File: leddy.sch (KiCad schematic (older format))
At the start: 98 parts, among them J1 hole 1, J2 hole 1, J3 hole 1, J4 hole 1, J5 umbrella hole, J6 PJ-002AH-SMT-TR, J7 OPEN HARDWARE, Q1 ZXMP6A13GTA, SW1 PTS645SM70SMTR92, U1 LT3518EFE#PBF, U2 74HC4017PW

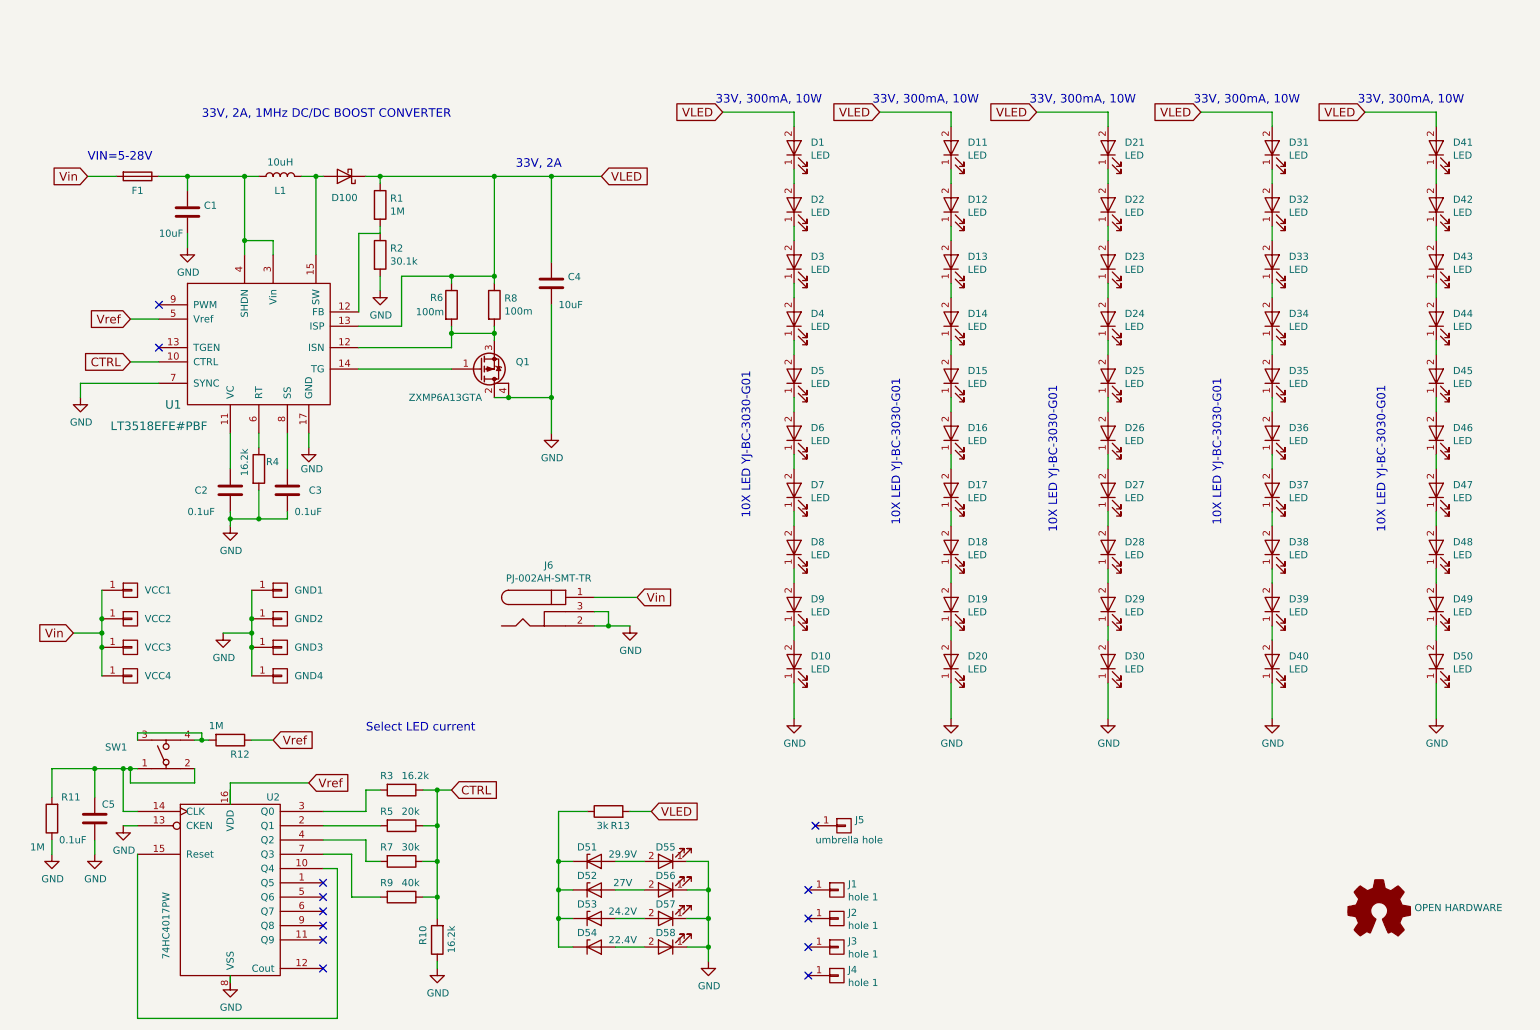
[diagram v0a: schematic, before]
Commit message: added better LED current level meter
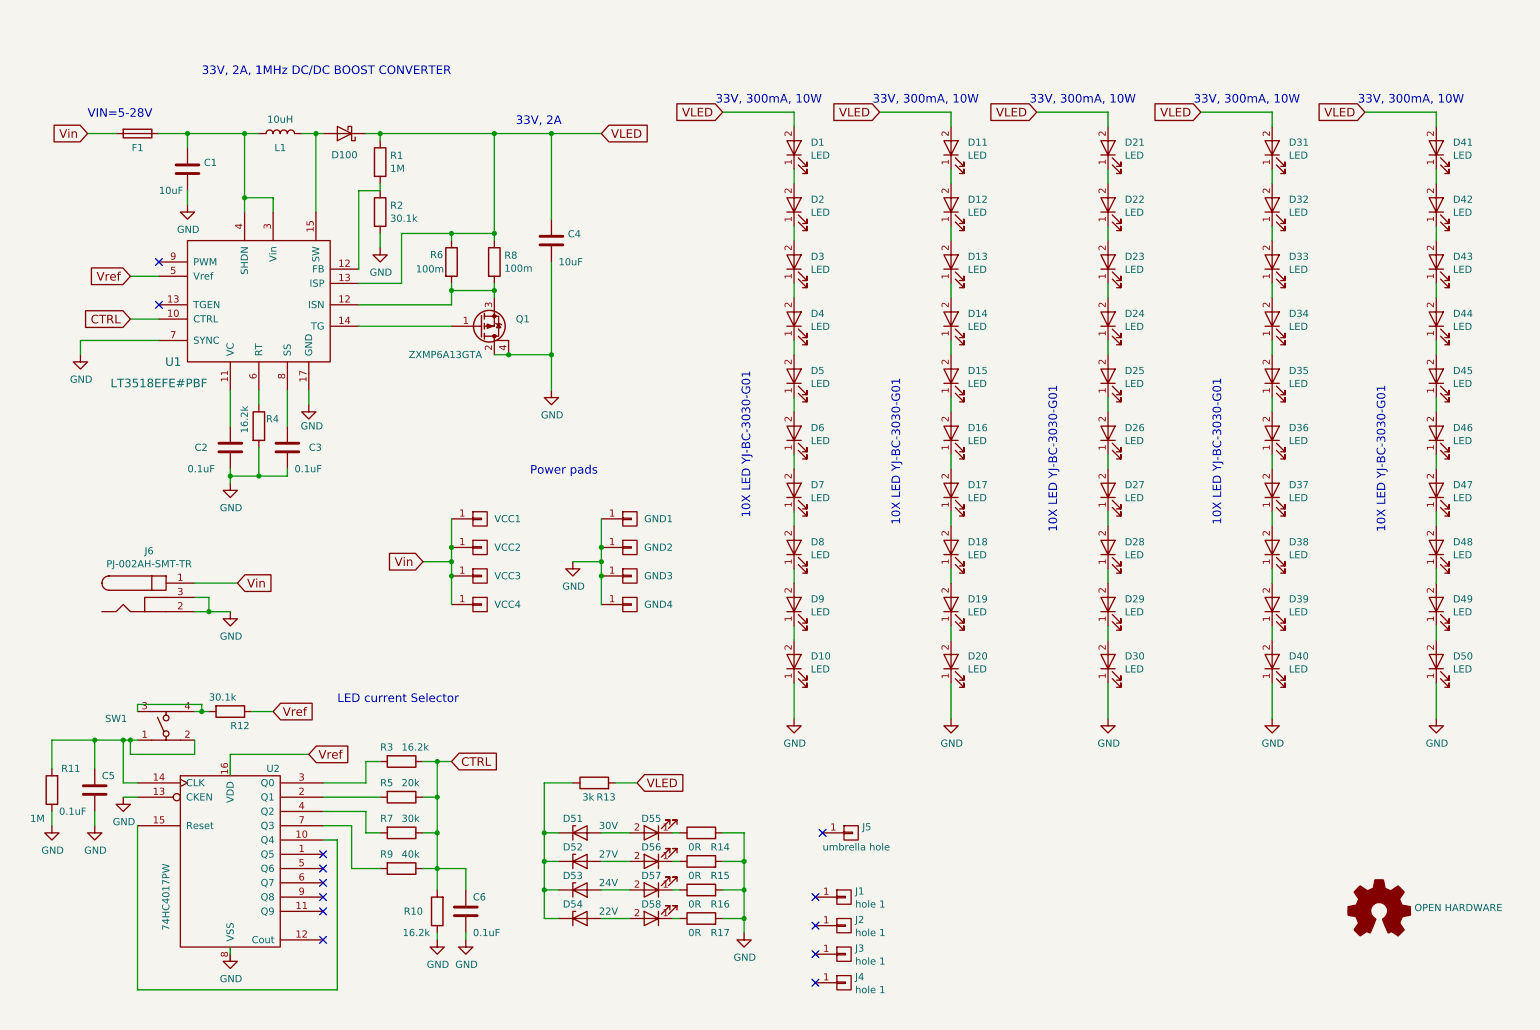
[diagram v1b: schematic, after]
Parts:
- added C6: 0.1uF, Capacitors_SMD:C_0603_HandSoldering, symbol C
- added R14, R15, R16, R17: 0R, Resistors_SMD:R_0603_HandSoldering, symbol R
- D51: value 29.9V -> 30V; Description Zener 29.9V 2mA 0603 -> Zener 30V 2mA 0603
- D53: value 24.2V -> 24V; Description Zener 24.2V 2mA 0603 -> Zener 24V 2mA 0603
- D54: value 22.4V -> 22V; Description Zener 22.4V 2mA 0603 -> Zener 22V 2mA 0603
- R12: value 1M -> 30.1k; Description RES 1M 1% 0603 -> RES 30.1k 1% 0603
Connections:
- net CTRL: now also C6.1
- net GND: now also C6.2, R14.2, R15.2, R16.2, R17.2; no longer D55.1 (K), D56.1 (K), D57.1 (K), D58.1 (K)
- new net: D55.1 (K), R14.1
- new net: D56.1 (K), R15.1
- new net: D57.1 (K), R16.1
- new net: D58.1 (K), R17.1
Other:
- note added: "LED current Selector"
- note added: "Power pads"
- note removed: "Select LED current"
- moved on the sheet: C1, C2, C3, C4, C5, D100, D51, D52, D53, D54, D55, D56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

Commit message: total power is now 60W and there are 6 level of led power regulation
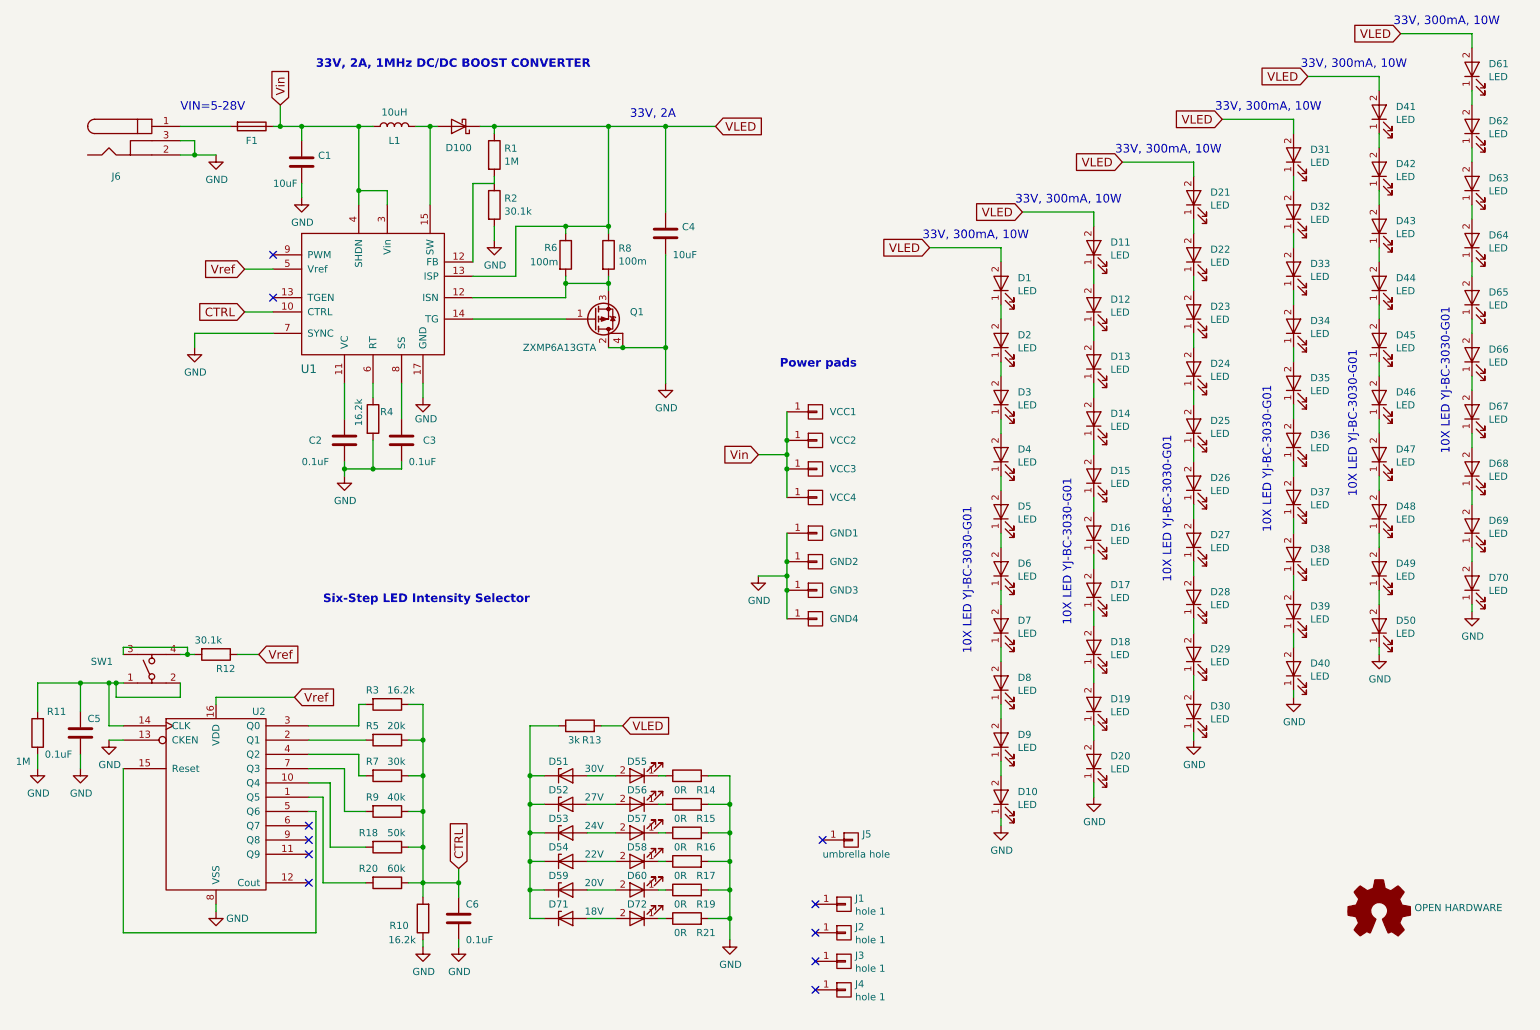
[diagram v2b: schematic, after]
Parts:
- added D59: 20V, Diodes_SMD:D_0603, symbol D_Zener
- added D60, D72: LED, lib:LED_PLCC-2, symbol LED
- added D61, D62, D63, D64, D65, D66, D67, D68, D69, D70: LED, lib:LED-3030, symbol LED
- added D71: 18V, Diodes_SMD:D_0603, symbol D_Zener
- added R18: 50k, Resistors_SMD:R_0603_HandSoldering, symbol R
- added R19, R21: 0R, Resistors_SMD:R_0603_HandSoldering, symbol R
- added R20: 60k, Resistors_SMD:R_0603_HandSoldering, symbol R
- D1, D10, D11, D12, D13, D14, D15, D16, D17, D18, D19, D2, D20, D21, D22, D23, D24, D25, D26, D27, D28, D29, D3, D30, D31, D32, D33, D34, D35, D36, D37, D38, D39, D4, D40, D41, D42, D43, D44, D45, D46, D47, D48, D49, D5, D50, D6, D7, D8, D9: Description (none) -> Hi CRI LED
- F1: Description Fuse 10A -> Fuse 10A, 32V
- GND1, GND2, GND3, GND4: Description 3.2mm mounting hole -> GND power pad DO NOT FIT
- J1, J2, J3, J4: Description 3.2mm mounting hole -> 3.2mm mounting hole, DO NOT FIT
- J5: Description 3.2mm mounting hole -> large umbrella hole, DO NOT FIT
- J7: Description (none) -> Open Hardware Logo, DO NOT FIT
- L1: Description (none) -> 10uH Inductor; SUP! Mouser -> (none); SUP1 (none) -> Mouser
- Q1: Description (none) -> MOS FET Transistor
- SW1: Description Tactile Switches 50mA 12VDC C&K Components PTS645SM70SMTR92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 -> Tactile Switches 50mA 12VDC
- VCC1, VCC2, VCC3, VCC4: Description 3.2mm mounting hole -> Power pad, DO NOT FIT
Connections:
- net CTRL: now also R18.1, R20.1
- net GND: now also U2.8 (VSS), D70.1 (K), R19.2, R21.2
- net VLED: now also D61.2 (A)
- net Vin: now also C1.1, F1.1, L1.1, U1.3 (Vin), U1.4 (SHDN); no longer F1.2, J6.1
- net Vref: now also U2.16 (VDD)
- net at U2.1 (Q5): now also R20.2
- net at U2.10 (Q4): now also R18.2; no longer U2.15 (Reset)
- net at U2.5 (Q6): now also U2.15 (Reset)
- net at D51.1 (K), D52.1 (K), D53.1 (K)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: now also D59.1 (K), D71.1 (K)
- new net: F1.2, J6.1
- new net: D60.1 (K), R19.1
- new net: D59.2 (A), D60.2 (A)
- new net: D66.1 (K), D67.2 (A)
- new net: D65.1 (K), D66.2 (A)
- new net: D67.1 (K), D68.2 (A)
- new net: D68.1 (K), D69.2 (A)
- new net: D69.1 (K), D70.2 (A)
- new net: D64.1 (K), D65.2 (A)
- new net: D63.1 (K), D64.2 (A)
- new net: D62.1 (K), D63.2 (A)
- new net: D61.1 (K), D62.2 (A)
- new net: D72.1 (K), R21.1
- new net: D71.2 (A), D72.2 (A)
- no-connect marks 13 -> 11
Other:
- note added: "Six-Step LED Intensity Selector"
- note removed: "LED current Selector"
- moved on the sheet: C1, C2, C3, C4, C5, C6, D1, D10, D100, D11, D12, D13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
